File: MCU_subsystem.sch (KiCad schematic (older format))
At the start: 1 part

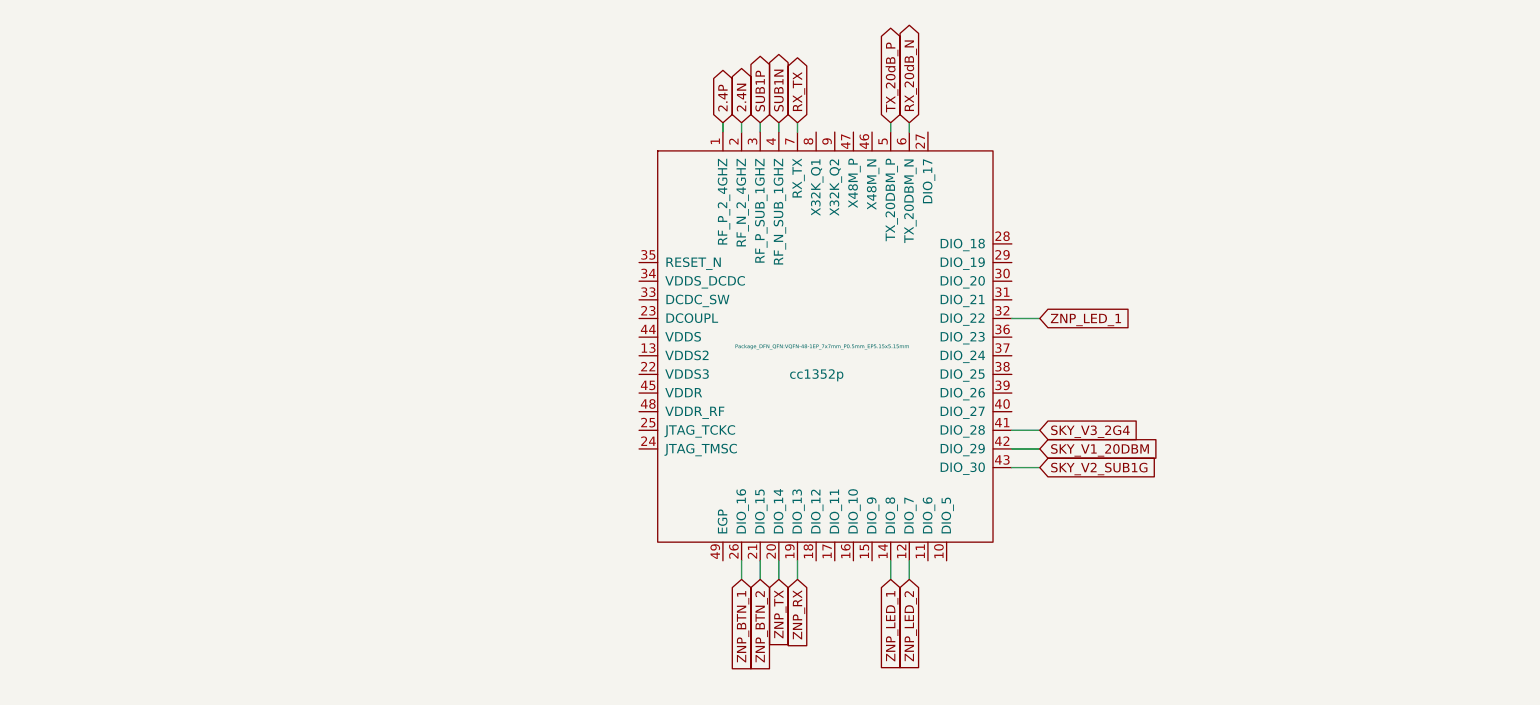
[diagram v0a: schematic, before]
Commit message: Finished Adding MCU connections and combined crystal and MCU sheets.
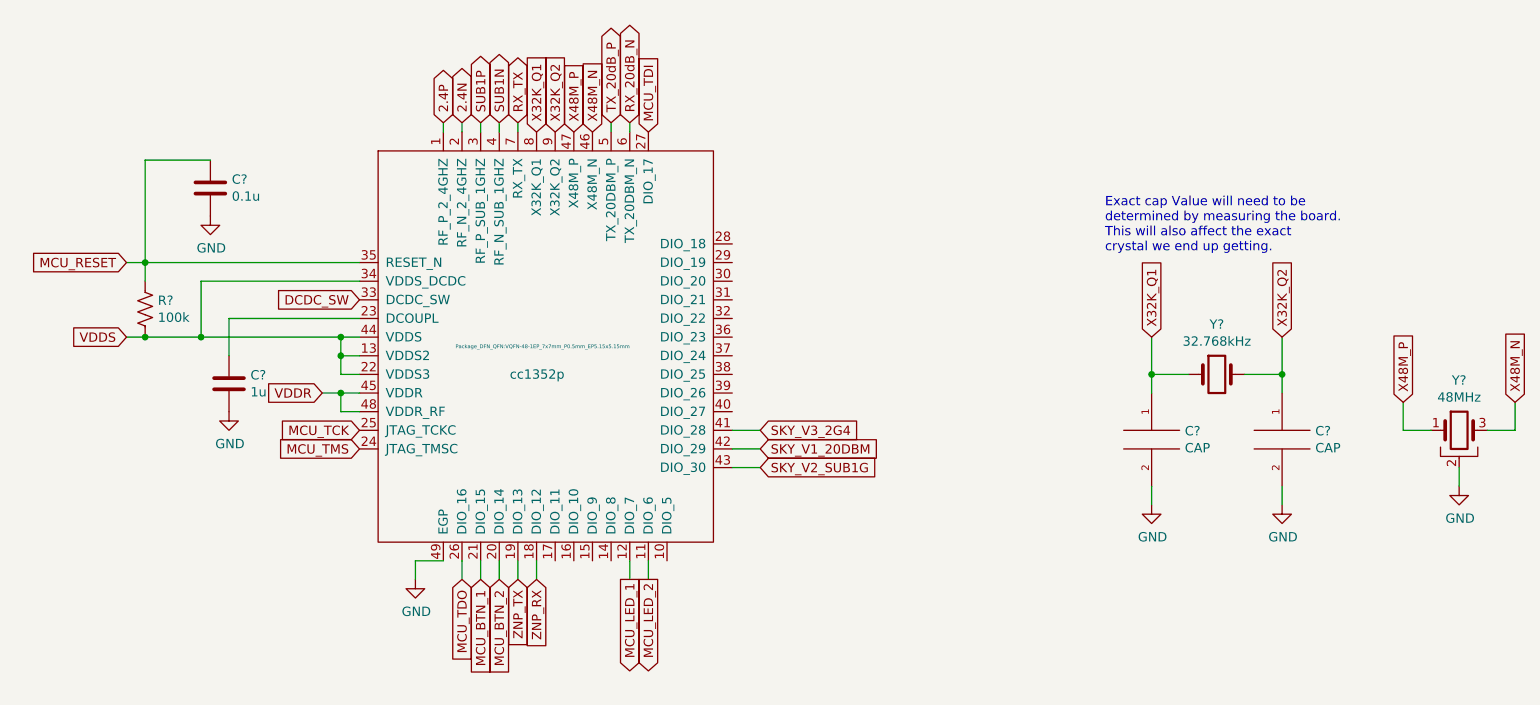
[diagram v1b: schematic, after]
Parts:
- added C?: 1u, symbol Device:C
- added C?: 0.1u, symbol Device:C
- added C? (x2): CAP, Capacitor_SMD:C_0805_2012Metric_Pad1.18x1.45mm_HandSolder, symbol pspice:CAP
- added R?: 100k, symbol Device:R_US
- added Y?: 32.768kHz, Crystal:Crystal_SMD_2012-2Pin_2.0x1.2mm_HandSoldering, symbol Device:Crystal
- added Y?: 48MHz, Crystal:Crystal_SMD_2016-4Pin_2.0x1.6mm, symbol Device:Crystal_GND2
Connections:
- net ZNP_RX: now also U?.18 (DIO_12); no longer U?.19 (DIO_13)
- net ZNP_TX: now also U?.19 (DIO_13); no longer U?.20 (DIO_14)
- net MCU_LED_2: now reaches U?.11 (DIO_6)
- net VDDS: now reaches U?.13 (VDDS2)
- net VDDS: now also U?.22 (VDDS3), U?.34 (VDDS_DCDC), U?.44 (VDDS), R?.2
- net at U?.23 (DCOUPL): now also C?.1
- net MCU_TMS: now reaches U?.24 (JTAG_TMSC)
- net MCU_TCK: now reaches U?.25 (JTAG_TCKC)
- net MCU_TDI: now reaches U?.27 (DIO_17)
- net DCDC_SW: now reaches U?.33 (DCDC_SW)
- net MCU_RESET: now reaches U?.35 (RESET_N)
- net MCU_RESET: now also C?.1, R?.1
- net VDDR: now reaches U?.45 (VDDR)
- net VDDR: now also U?.48 (VDDR_RF)
- net X48M_N: now reaches U?.46 (X48M_N)
- net X48M_N: now also Y?.3
- net X48M_P: now reaches U?.47 (X48M_P)
- net X48M_P: now also Y?.1
- net GND: now reaches U?.49 (EGP)
- net GND: now also C?.2, C?.2, C?.2, C?.2, Y?.2
- net X32K_Q1: now reaches U?.8 (X32K_Q1)
- net X32K_Q1: now also C?.1, Y?.1
- net X32K_Q2: now reaches U?.9 (X32K_Q2)
- net X32K_Q2: now also C?.1, Y?.2
- net ZNP_BTN_1 renamed MCU_TDO
- net ZNP_BTN_2 renamed MCU_BTN_1
- net ZNP_LED_1: no longer names the net of U?.14 (DIO_8)
- net ZNP_LED_1: no longer U?.32 (DIO_22)
- net ZNP_LED_2 renamed MCU_LED_1
- new net MCU_BTN_2: U?.20 (DIO_14)
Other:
- note added: "Exact cap Value will need to be \ndetermined by measuring the board. \nThis will also affect the exact \ncrystal we end up getting."

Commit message: part way through PCB rework using new components. 62 unconnected.
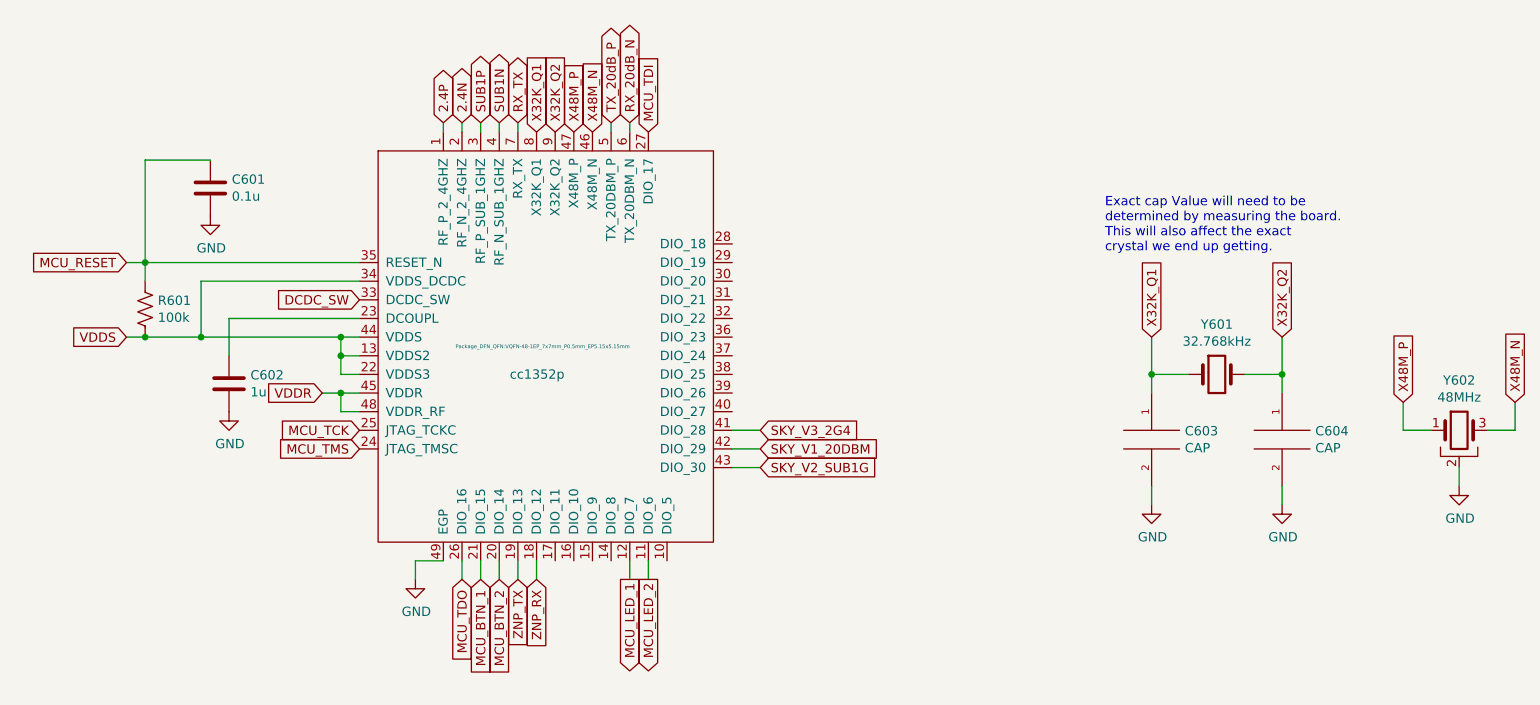
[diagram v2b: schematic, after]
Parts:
- gave numbers to parts that had none: 8
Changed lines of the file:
@@
 P 2950 4900
 AR Path="/60365D6B/614C4674" Ref="U?"  Part="1"
-AR Path="/614C2CA1/614C4674" Ref="U?"  Part="1"
-F 0 "U?" H 4109 4154 50  0001 C BNN
+AR Path="/614C2CA1/614C4674" Ref="U601"  Part="1"
+F 0 "U601" H 4109 4154 50  0001 C BNN
 F 1 "cc1352p" H 3950 5800 50  0000 R CNN
 F 2 "Package_DFN_QFN:VQFN-48-1EP_7x7mm_P0.5mm_EP5.15x5.15mm" H 4300 5950 20  0000 R CNN
@@
 SKY_V1_20DBM
 $Comp
-L power:GND #PWR?
+L power:GND #PWR0602
 U 1 1 614C8FCE
 P 2150 4200
-F 0 "#PWR?" H 2150 3950 50  0001 C CNN
+F 0 "#PWR0602" H 2150 3950 50  0001 C CNN
 F 1 "GND" H 2155 4027 50  0000 C CNN
 F 2 "" H 2150 4200 50  0001 C CNN
@@
 	2750 4100 2650 4100
 $Comp
-L Device:R_US R?
+L Device:R_US R601
 U 1 1 614CB248
 P 1700 3650
-F 0 "R?" H 1768 3696 50  0000 L CNN
+F 0 "R601" H 1768 3696 50  0000 L CNN
 F 1 "100k" H 1768 3605 50  0000 L CNN
 F 2 "" V 1740 3640 50  0001 C CNN
@@
 Connection ~ 2000 3800
 $Comp
-L Device:C C?
+L Device:C C602
 U 1 1 614CF3BD
 P 2150 4050
-F 0 "C?" H 2265 4096 50  0000 L CNN
+F 0 "C602" H 2265 4096 50  0000 L CNN
 F 1 "1u" H 2265 4005 50  0000 L CNN
 F 2 "" H 2188 3900 50  0001 C CNN
@@
 Connection ~ 1700 3400
 $Comp
-L Device:C C?
+L Device:C C601
 U 1 1 614D5273
 P 2050 3000
-F 0 "C?" H 2165 3046 50  0000 L CNN
+F 0 "C601" H 2165 3046 50  0000 L CNN
 F 1 "0.1u" H 2165 2955 50  0000 L CNN
 F 2 "" H 2088 2850 50  0001 C CNN
@@
 $EndComp
 $Comp
-L power:GND #PWR?
+L power:GND #PWR0601
 U 1 1 614D592A
 P 2050 3150
-F 0 "#PWR?" H 2050 2900 50  0001 C CNN
+F 0 "#PWR0601" H 2050 2900 50  0001 C CNN
 F 1 "GND" H 2055 2977 50  0000 C CNN
 F 2 "" H 2050 3150 50  0001 C CNN
@@
 	1700 2850 2050 2850
 $Comp
-L power:GND #PWR?
+L power:GND #PWR0603
 U 1 1 614DC14A
 P 3150 5100
-F 0 "#PWR?" H 3150 4850 50  0001 C CNN
+F 0 "#PWR0603" H 3150 4850 50  0001 C CNN
 F 1 "GND" H 3155 4927 50  0000 C CNN
 F 2 "" H 3150 5100 50  0001 C CNN
@@
 P 7450 4000
 AR Path="/613805C9/614E7AAF" Ref="Y?"  Part="1"
-AR Path="/614C2CA1/614E7AAF" Ref="Y?"  Part="1"
-F 0 "Y?" H 7450 4268 50  0000 C CNN
+AR Path="/614C2CA1/614E7AAF" Ref="Y601"  Part="1"
+F 0 "Y601" H 7450 4268 50  0000 C CNN
 F 1 "32.768kHz" H 7450 4177 50  0000 C CNN
 F 2 "Crystal:Crystal_SMD_2012-2Pin_2.0x1.2mm_HandSoldering" H 7450 4000 50  0001 C CNN
@@
 P 8750 4300
 AR Path="/613805C9/614E7AB5" Ref="Y?"  Part="1"
-AR Path="/614C2CA1/614E7AB5" Ref="Y?"  Part="1"
-F 0 "Y?" H 8750 4568 50  0000 C CNN
+AR Path="/614C2CA1/614E7AB5" Ref="Y602"  Part="1"
+F 0 "Y602" H 8750 4568 50  0000 C CNN
 F 1 "48MHz" H 8750 4477 50  0000 C CNN
 F 2 "Crystal:Crystal_SMD_2016-4Pin_2.0x1.6mm" H 8750 4300 50  0001 C CNN
@@
 P 7100 4350
 AR Path="/613805C9/614E7ABB" Ref="C?"  Part="1"
-AR Path="/614C2CA1/614E7ABB" Ref="C?"  Part="1"
-F 0 "C?" H 7278 4396 50  0000 L CNN
+AR Path="/614C2CA1/614E7ABB" Ref="C603"  Part="1"
+F 0 "C603" H 7278 4396 50  0000 L CNN
 F 1 "CAP" H 7278 4305 50  0000 L CNN
 F 2 "Capacitor_SMD:C_0805_2012Metric_Pad1.18x1.45mm_HandSolder" H 7100 4350 50  0001 C CNN
@@
 P 7800 4350
 AR Path="/613805C9/614E7AC1" Ref="C?"  Part="1"
-AR Path="/614C2CA1/614E7AC1" Ref="C?"  Part="1"
-F 0 "C?" H 7978 4396 50  0000 L CNN
+AR Path="/614C2CA1/614E7AC1" Ref="C604"  Part="1"
+F 0 "C604" H 7978 4396 50  0000 L CNN
 F 1 "CAP" H 7978 4305 50  0000 L CNN
 F 2 "Capacitor_SMD:C_0805_2012Metric_Pad1.18x1.45mm_HandSolder" H 7800 4350 50  0001 C CNN
@@
 P 8750 4600
 AR Path="/613805C9/614E7ACB" Ref="#PWR?"  Part="1"
-AR Path="/614C2CA1/614E7ACB" Ref="#PWR?"  Part="1"
-F 0 "#PWR?" H 8750 4350 50  0001 C CNN
+AR Path="/614C2CA1/614E7ACB" Ref="#PWR0606"  Part="1"
+F 0 "#PWR0606" H 8750 4350 50  0001 C CNN
 F 1 "GND" H 8755 4427 50  0000 C CNN
 F 2 "" H 8750 4600 50  0001 C CNN
@@
 P 7800 4700
 AR Path="/613805C9/614E7AD1" Ref="#PWR?"  Part="1"
-AR Path="/614C2CA1/614E7AD1" Ref="#PWR?"  Part="1"
-F 0 "#PWR?" H 7800 4450 50  0001 C CNN
+AR Path="/614C2CA1/614E7AD1" Ref="#PWR0605"  Part="1"
+F 0 "#PWR0605" H 7800 4450 50  0001 C CNN
 F 1 "GND" H 7805 4527 50  0000 C CNN
 F 2 "" H 7800 4700 50  0001 C CNN
@@
 P 7100 4700
 AR Path="/613805C9/614E7AD7" Ref="#PWR?"  Part="1"
-AR Path="/614C2CA1/614E7AD7" Ref="#PWR?"  Part="1"
-F 0 "#PWR?" H 7100 4450 50  0001 C CNN
+AR Path="/614C2CA1/614E7AD7" Ref="#PWR0604"  Part="1"
+F 0 "#PWR0604" H 7100 4450 50  0001 C CNN
 F 1 "GND" H 7105 4527 50  0000 C CNN
 F 2 "" H 7100 4700 50  0001 C CNN
